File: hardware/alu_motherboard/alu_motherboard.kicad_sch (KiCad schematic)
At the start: 69 parts, among them J2 Conn_02x26_Odd_Even, J3 ADD_SUB, J4 BITOPS, J5 SHIFT, Q10 IRLML6244, Q11 IRLML6244, Q12 IRLML6244, Q13 IRLML6244, Q14 IRLML6244, Q15 IRLML6244, Q16 IRLML6244, Q3 IRLML6244, Q4 IRLML6244, Q5 IRLML6244, Q6 IRLML6244, Q9 IRLML6244, U2 74HC00, U3 74HC00, U4 74HC00, U5 74HC00, U6 74HC00

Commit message: more ALU motherboard feedback
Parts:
- added D21: LED, LED_SMD:LED_0603_1608Metric_Pad1.05x0.95mm_HandSolder, symbol Device:LED
- added R20: 1000, Resistor_SMD:R_0603_1608Metric_Pad0.98x0.95mm_HandSolder, symbol Device:R
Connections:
- net +5V: now also D21.2 (A)
- net GND: now also R20.2
- new net: D21.1 (K), R20.1

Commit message: fixed mux include
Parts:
- renumbered C22 to C1, C20 to C10, C21 to C11, C23 to C2, C24 to C3, C25 to C4, C26 to C5, C27 to C6, C17 to C7, C18 to C8, C19 to C9, D21 to D1, D4 to D10, D3 to D11, D2 to D12, D1 to D13, D13 to D14, D14 to D15, D15 to D16, D16 to D17, D17 to D18, D18 to D19, D10 to D2, D19 to D20, D20 to D21, D11 to D3, D9 to D4, D12 to D5, D8 to D6, D6 to D8, D5 to D9, J3 to J1, J4 to J3, J5 to J4, Q4 to Q1, Q14 to Q10, Q15 to Q11, Q16 to Q12, Q5 to Q2, Q6 to Q4, Q9 to Q5, Q10 to Q6, Q11 to Q7, Q12 to Q8, Q13 to Q9, R20 to R1, R15 to R10, R16 to R11, R17 to R12, R18 to R13, R19 to R14, R6 to R2, R7 to R3, R5 to R4, R8 to R5, R4 to R6, R12 to R7, R13 to R8, R14 to R9, U6 to U1
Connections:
- net 8Bit_Mux1/RES0 renamed 8Bit_Mux3/RES0
- net 8Bit_Mux1/RES1 renamed 8Bit_Mux3/RES1
- net 8Bit_Mux1/RES2 renamed 8Bit_Mux3/RES2
- net 8Bit_Mux1/RES3 renamed 8Bit_Mux3/RES3
- net 8Bit_Mux1/RES4 renamed 8Bit_Mux3/RES4
- net 8Bit_Mux1/RES5 renamed 8Bit_Mux3/RES5
- net 8Bit_Mux1/RES6 renamed 8Bit_Mux3/RES6
- net 8Bit_Mux1/RES7 renamed 8Bit_Mux3/RES7
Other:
- removed sheet 8Bit_Mux1
- added sheet 8Bit_Mux3 (mux.kicad_sch)
- sheet 8Bit_Mux2: file ../alu_shift/mux.kicad_sch -> mux.kicad_sch

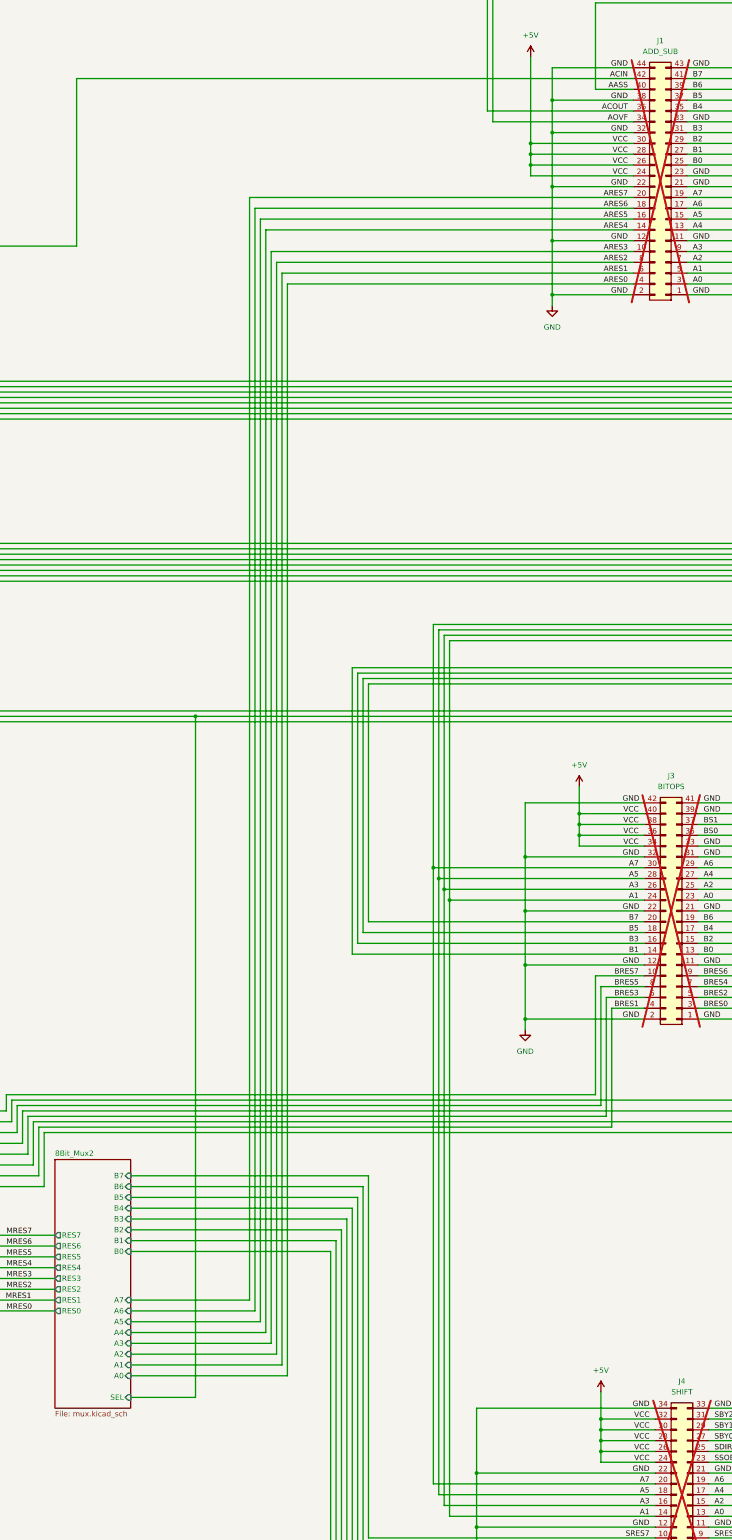
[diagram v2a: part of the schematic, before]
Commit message: ALU shifter, bitops and motherboard as ordered
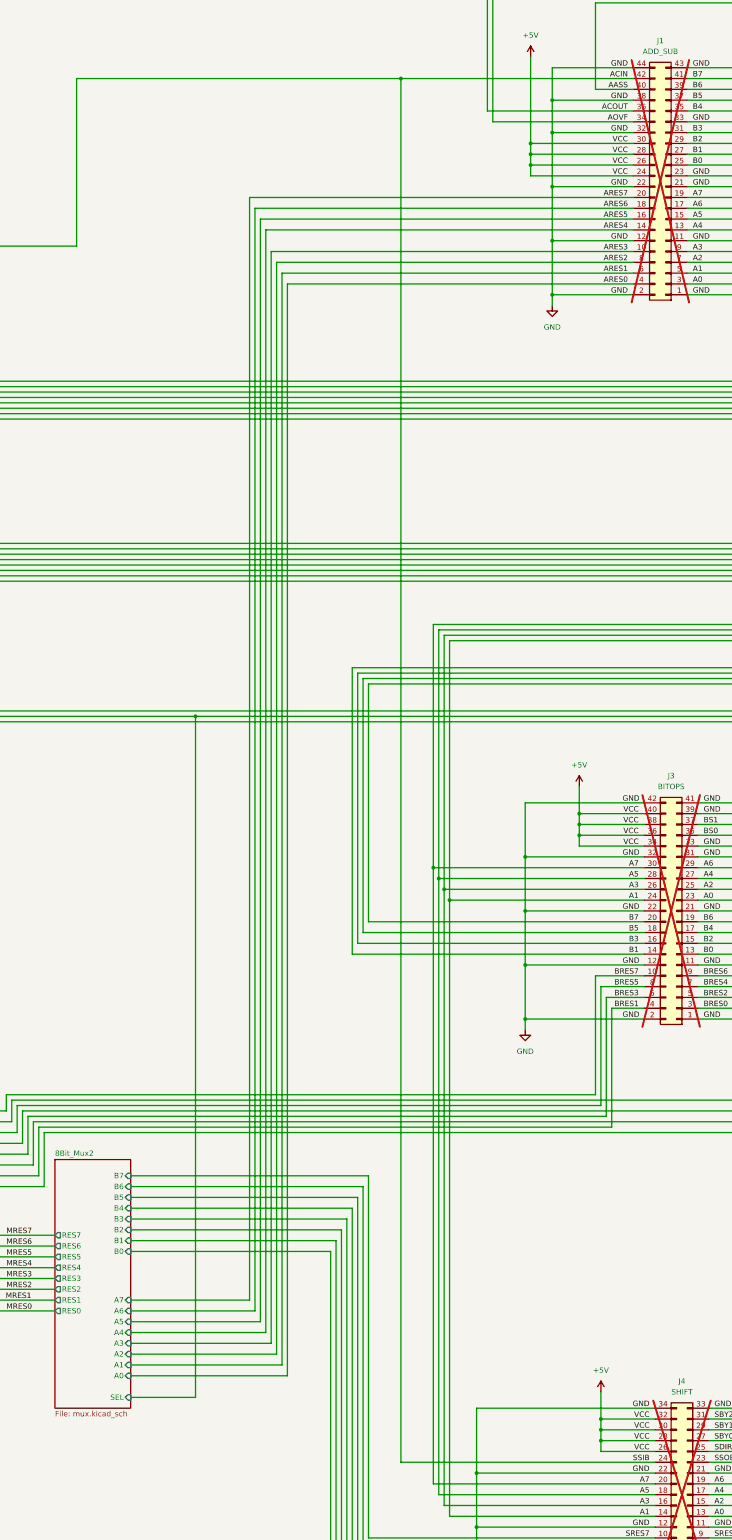
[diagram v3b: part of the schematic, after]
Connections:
- net +5V: no longer J4.24 (Pin_24)
- net ACIN: now also J4.24 (Pin_24)
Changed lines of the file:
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@@
 	)
 	(junction
-		(at 411.48 382.27)
-		(diameter 0)
-		(color 0 0 0 0)
-	)
-	(junction
 		(at 683.26 448.31)
 		(diameter 0)
@@
 	)
 	(junction
+		(at 364.49 59.69)
+		(diameter 0)
+		(color 0 0 0 0)
+	)
+	(junction
 		(at 786.13 422.91)
 		(diameter 0)
@@
 	(wire
 		(pts
-			(xy 288.29 59.69) (xy 419.1 59.69)
+			(xy 288.29 59.69) (xy 364.49 59.69)
 		)
 		(stroke
@@
 	(wire
 		(pts
+			(xy 364.49 59.69) (xy 419.1 59.69)
+		)
+		(stroke
+			(width 0)
+			(type default)
+		)
+	)
+	(wire
+		(pts
 			(xy 744.22 388.62) (xy 756.92 388.62)
 		)
@@
 	(wire
 		(pts
-			(xy 424.18 384.81) (xy 411.48 384.81)
-		)
-		(stroke
-			(width 0)
-			(type default)
-		)
-	)
-	(wire
-		(pts
 			(xy 116.84 265.43) (xy 121.92 265.43)
 		)
@@
 	(wire
 		(pts
+			(xy 364.49 59.69) (xy 364.49 384.81)
+		)
+		(stroke
+			(width 0)
+			(type default)
+		)
+	)
+	(wire
+		(pts
 			(xy 480.06 130.81) (xy 480.06 187.96)
 		)
@@
 	(wire
 		(pts
+			(xy 364.49 384.81) (xy 424.18 384.81)
+		)
+		(stroke
+			(width 0)
+			(type default)
+		)
+	)
+	(wire
+		(pts
 			(xy 215.9 96.52) (xy 215.9 99.06)
 		)
@@
 	(wire
 		(pts
-			(xy 411.48 382.27) (xy 411.48 384.81)
-		)
-		(stroke
-			(width 0)
-			(type default)
-		)
-	)
-	(wire
-		(pts
 			(xy 483.87 247.65) (xy 434.34 247.65)
 		)
@@
 		)
 	)
-	(label "VCC"
+	(label "SSIB"
 		(at 422.91 384.81 180)
 		(effects
